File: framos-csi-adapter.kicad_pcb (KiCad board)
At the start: 4 copper layers, 26.5 x 26.5 mm, 71 parts, among them J1 DF40C-60DS-0.4V(51), J2 MSAK24025P30, U1 NTS0102GT, U2 AP62301Z6-7, U3 AP62301Z6-7

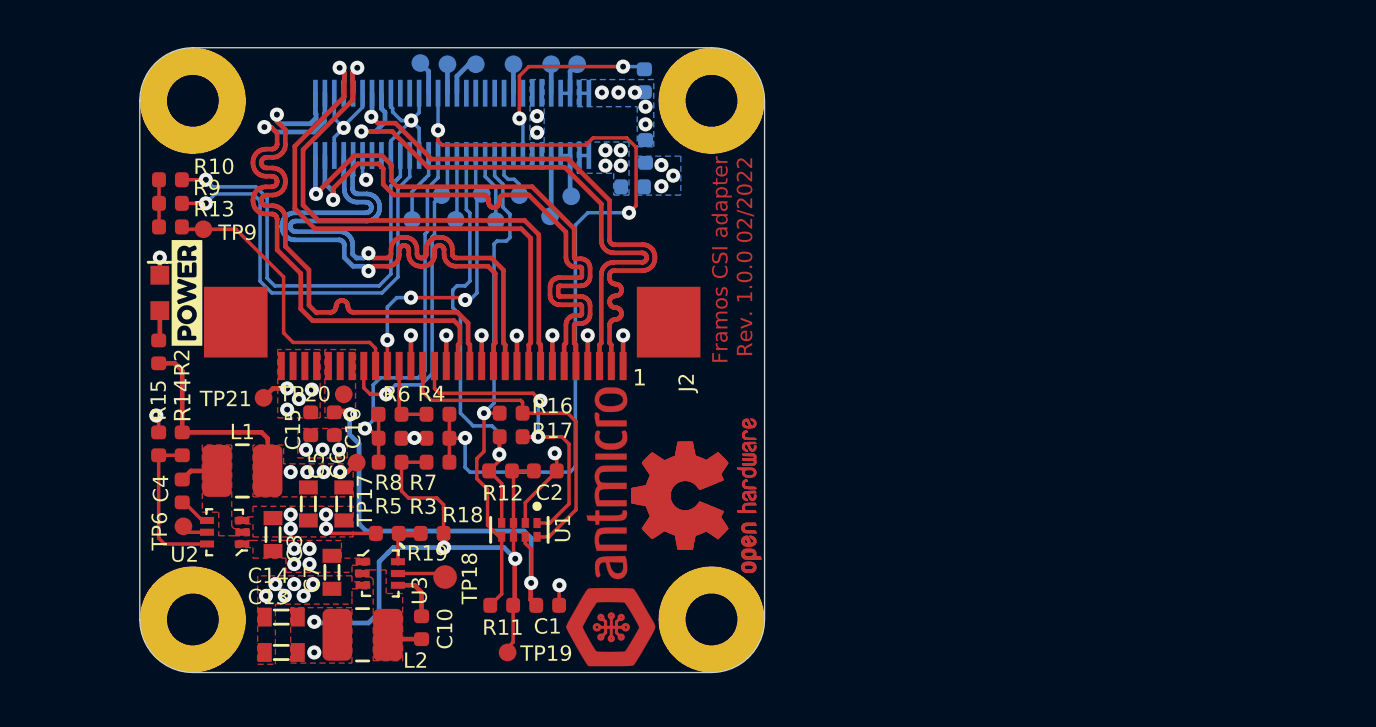
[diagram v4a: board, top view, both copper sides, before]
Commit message: Fixed diff traces impedance
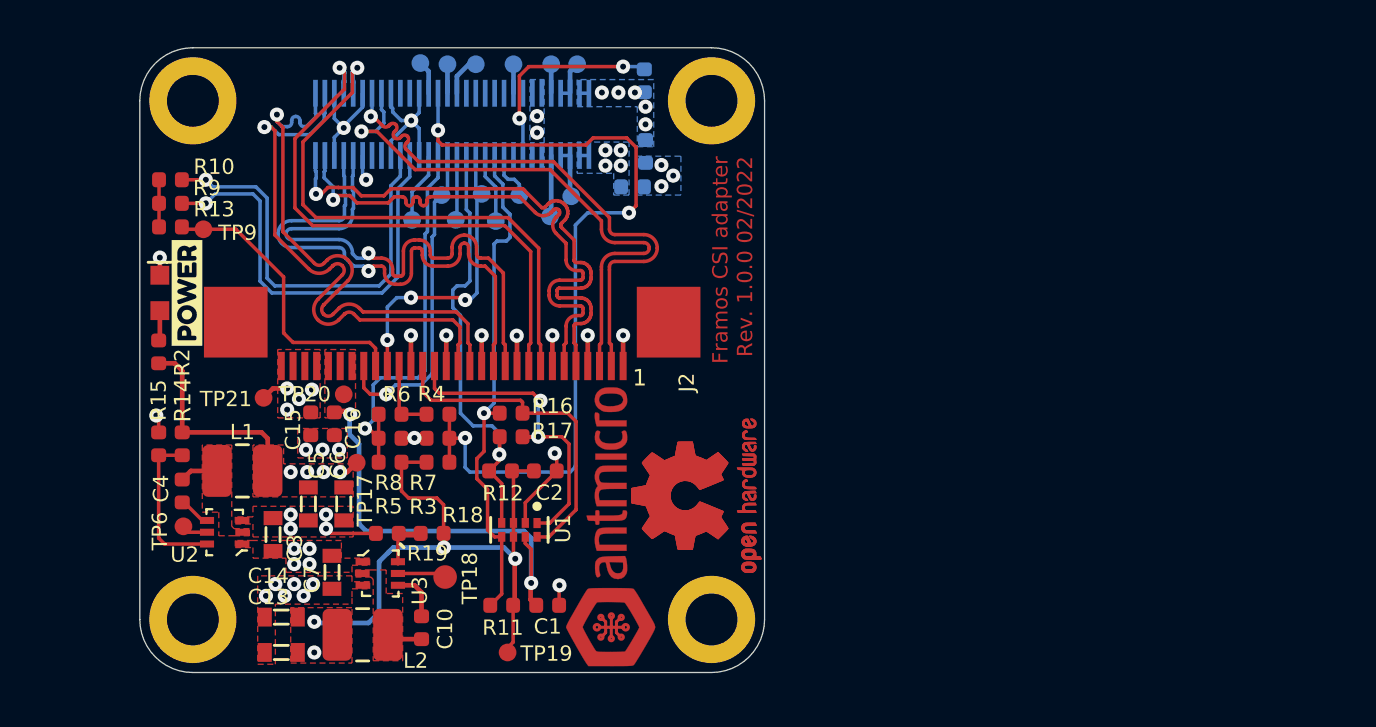
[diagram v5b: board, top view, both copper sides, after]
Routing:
- net CAM_SCL_3V3: track 15.0 -> 14.3 mm
- net CSI_D0_N: track 24.1 -> 23.5 mm
- net CSI_D0_P: track 24.1 -> 23.5 mm
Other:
- net class Default removed
- net class Z_100 removed
